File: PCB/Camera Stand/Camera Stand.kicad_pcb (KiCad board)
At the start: 2 copper layers, 149.9 x 106.7 mm, 40 parts, among them J1 Barrel_Jack, J2 HMC5883L, J3 Motor Drive, J4 Keypad 4x4, J5 Ultrasonic Left Front, J6 Ultrasonic Right Front, J7 Ultrasonic Left Back, J8 Ultrasonic Right Back, J9 GPS Module, K1 Relay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

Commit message: 3.3v error in PCB
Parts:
- DS1: value HY1602E LCD 16x2 -> HY1602E
- renumbered M1 to M5
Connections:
- C4 pad 1: /Atmega32/GND -> /Power Supply/3.3V
- C4 pad 2: /Power Supply/GND -> /Atmega32/GND
- C5 pad 2: /Power Supply/GND -> /Atmega32/GND
- J1 pad 2: /Power Supply/GND -> /Atmega32/GND
- J2 pad 1: /Atmega32/5V -> /Power Supply/3.3V
- J9 pad 1: /Atmega32/5V -> /Power Supply/3.3V
- U1 pad 2: /Atmega32/5V -> /Power Supply/3.3V
- U2 pad 2: /Power Supply/GND -> /Atmega32/GND
- U3 pad 2: /Power Supply/GND -> /Atmega32/GND
- U4 pad 1: /Atmega32/GND -> /Power Supply/3.3V
- U4 pad 2: /Power Supply/GND -> /Atmega32/GND
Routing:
- net /Power Supply/3.3V: track 0.00 -> 117.2 mm
- net /Power Supply/GND: track 79.0 -> 0.00 mm
- net /Atmega32/GND: track 358.2 -> 401.9 mm
- net /Atmega32/B0: track 82.1 -> 68.8 mm
- net Net-(J8-Pad3): track 20.4 -> 8.72 mm
- net /Atmega32/5V: track 358.9 -> 348.3 mm
- net /Atmega32/D6: track 50.0 -> 56.8 mm
- net /Atmega32/D4: track 17.0 -> 13.3 mm
- net Net-(J6-Pad2): track 35.3 -> 38.6 mm
- net /Atmega32/C7: track 33.2 -> 35.2 mm
- net Net-(J6-Pad3): track 26.1 -> 27.5 mm
- net Net-(C1-Pad1): track 37.5 -> 36.2 mm
- net /Power Supply/12V: track 39.1 -> 40.4 mm
- net Net-(J7-Pad2): track 31.1 -> 30.1 mm
- net /Atmega32/SDA: track 75.2 -> 74.3 mm
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
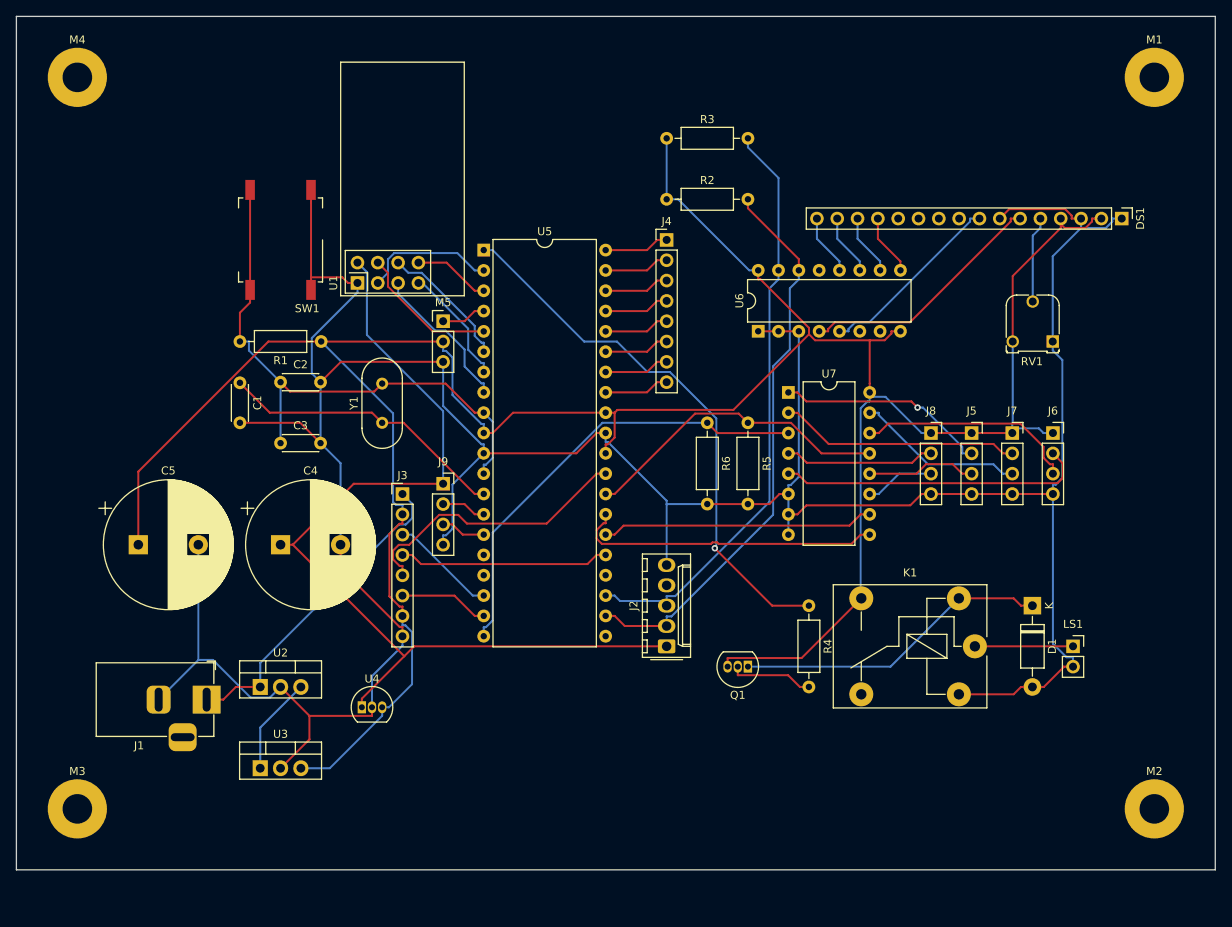
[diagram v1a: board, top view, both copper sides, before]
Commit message: 12v to siren
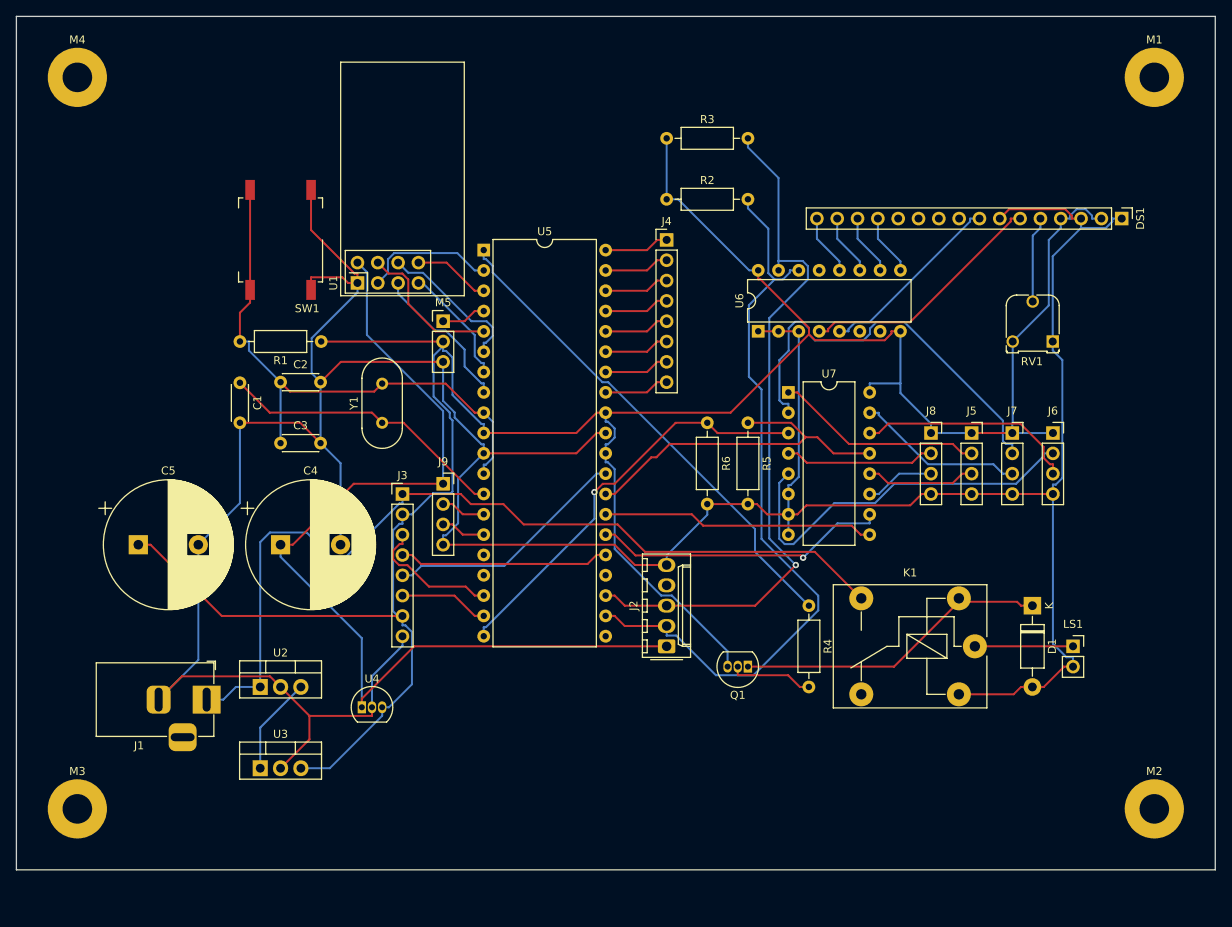
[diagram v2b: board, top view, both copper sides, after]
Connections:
- K1 pad 14: /Atmega32/5V -> /Power Supply/12V
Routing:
- net /Power Supply/12V: track 40.4 -> 111.7 mm
- net /Atmega32/GND: track 401.9 -> 425.8 mm
- net /Atmega32/SCL: track 71.3 -> 95.1 mm
- net Net-(J7-Pad2): track 30.1 -> 51.9 mm
- net /Atmega32/SDA: track 74.3 -> 89.2 mm, vias 0 -> 1
- net /Atmega32/5V: track 348.3 -> 337.8 mm
- net Net-(J6-Pad2): track 38.6 -> 48.0 mm
- net /Atmega32/B0: track 68.8 -> 61.9 mm, vias 1 -> 0
- net /Atmega32/C6: track 39.2 -> 44.7 mm
- net /Power Supply/3.3V: track 117.2 -> 122.0 mm
- net /Atmega32/C5: track 38.7 -> 34.1 mm
- net /Atmega32/C7: track 35.2 -> 30.7 mm
- net /Atmega32/D6: track 56.8 -> 52.3 mm, vias 0 -> 1
- net /Atmega32/D4: track 13.3 -> 17.0 mm
- net /Atmega32/C4: track 34.1 -> 37.1 mm, vias 0 -> 1
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
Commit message: Add simulation
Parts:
- moved C3 5.10 mm to (104.1, 93.9)
- moved J1 5.10 mm to (94.9, 125.9)
- moved J9 5.10 mm to (124.5, 98.9)
- moved Q1 5.10 mm to (162.6, 121.8)
- moved R1 5.10 mm to (109.2, 81.2)
- moved RV1 5.10 mm to (200.7, 81.2)
- moved U5 5.10 mm to (129.5, 69.7)
- moved J4 5.10 mm to (152.4, 68.5)
- moved M1 5.10 mm to (213.4, 48.1)
- moved M4 5.10 mm to (78.7, 48.1)
- moved R2 5.10 mm to (152.4, 63.4)
- moved R3 5.10 mm to (152.4, 55.8)
- moved SW1 5.10 mm to (104.1, 68.5)
- moved C1 5.10 mm to (99.1, 86.3)
- moved C2 5.10 mm to (104.1, 86.2)
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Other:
- board text added: "Group 47"
- board text added: "L1 Hardware Project"
